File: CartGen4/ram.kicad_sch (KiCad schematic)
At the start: 1 part

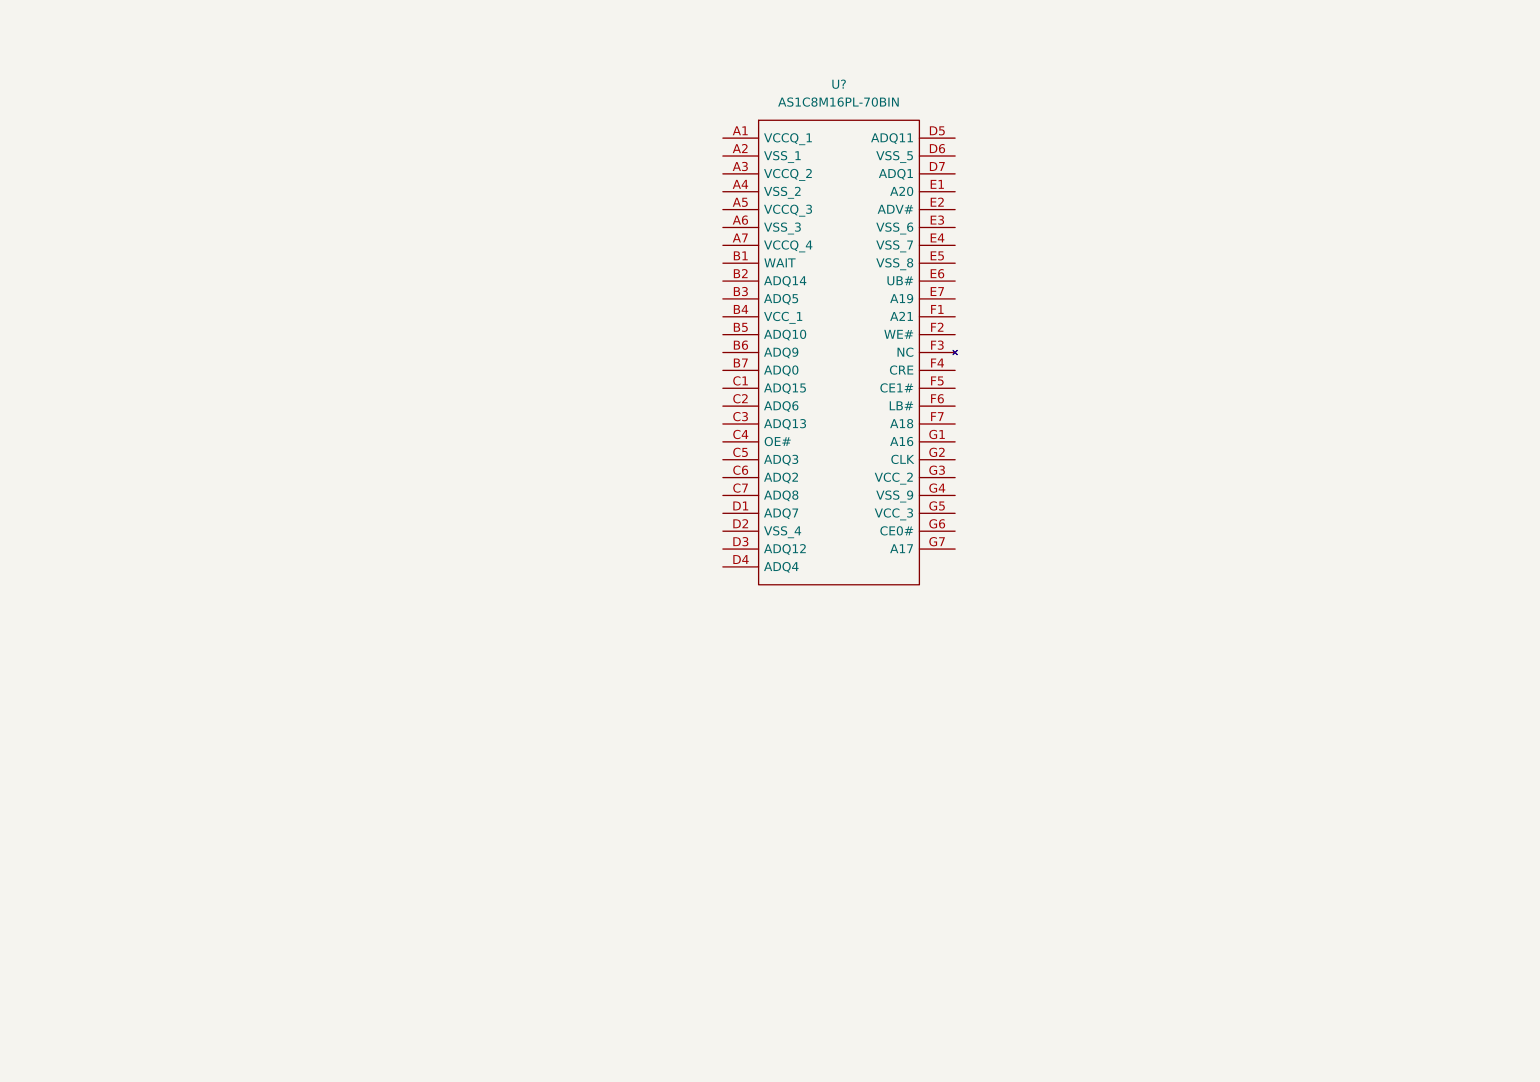
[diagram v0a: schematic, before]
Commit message: Added RAM and clock
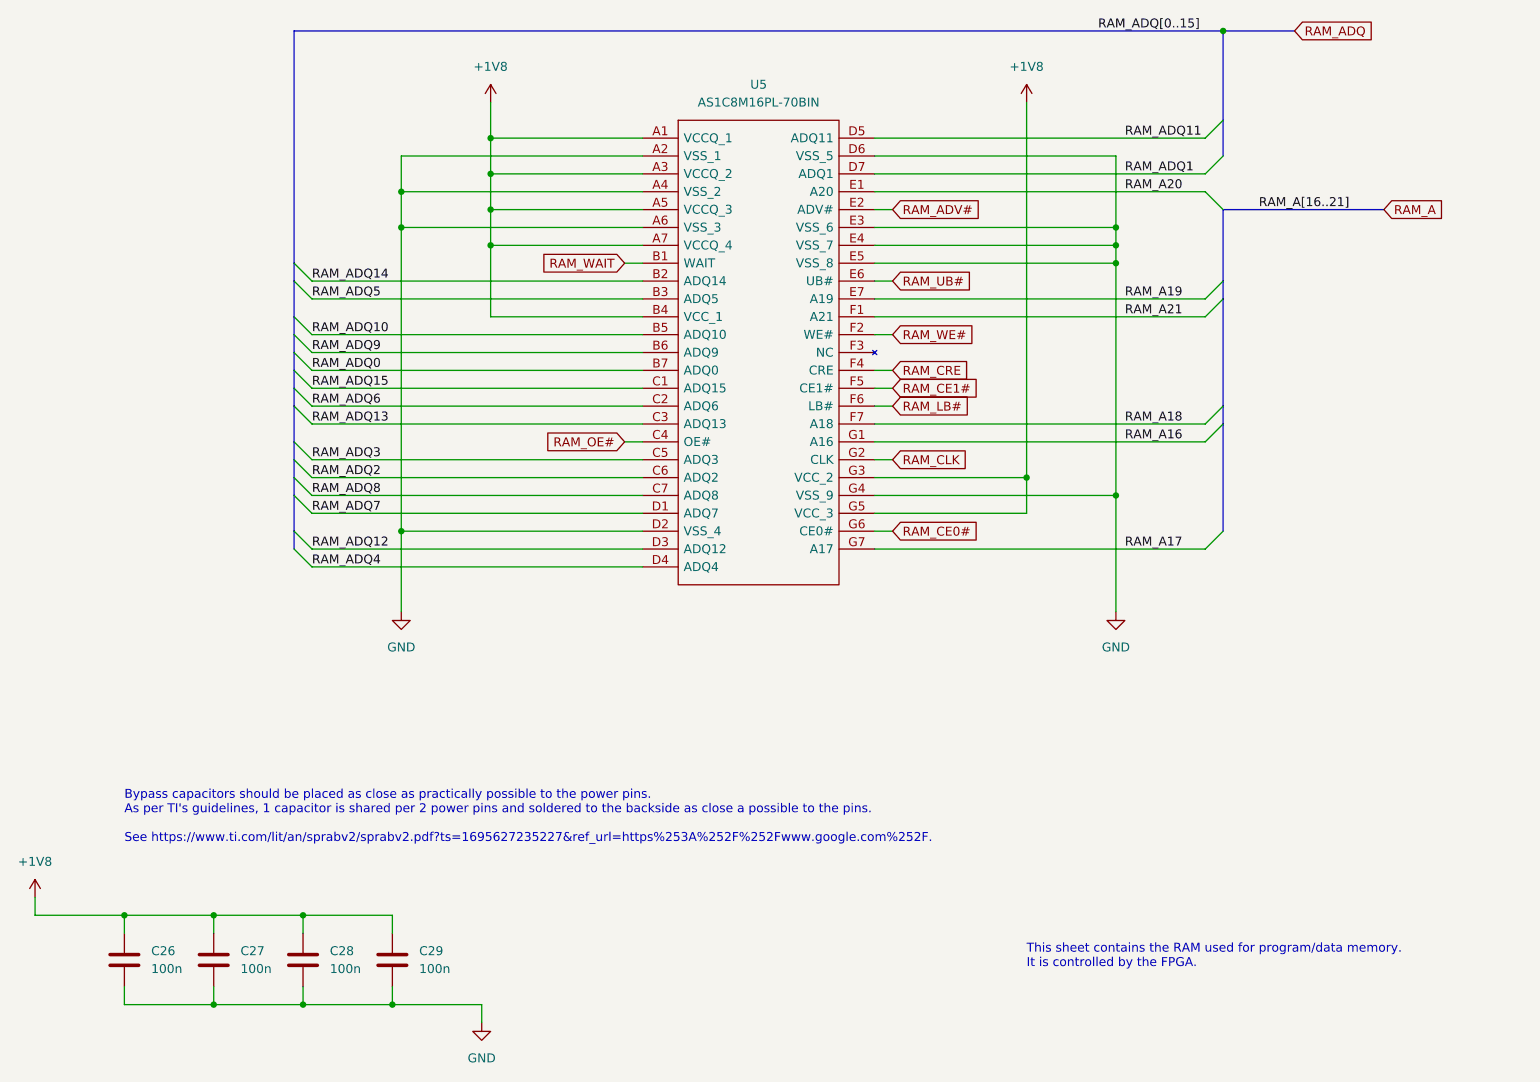
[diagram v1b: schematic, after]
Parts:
- added C26, C27, C28, C29: 100n, symbol Device:C
- gave numbers to parts that had none: 1
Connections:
- net +1V8: now reaches U5.A1 (VCCQ_1)
- net +1V8: now also U5.A3 (VCCQ_2), U5.A5 (VCCQ_3), U5.A7 (VCCQ_4), U5.B4 (VCC_1), U5.G3 (VCC_2), U5.G5 (VCC_3), C26.1, C27.1, C28.1, C29.1
- net GND: now reaches U5.A2 (VSS_1)
- net GND: now also U5.A4 (VSS_2), U5.A6 (VSS_3), U5.D2 (VSS_4), U5.D6 (VSS_5), U5.E3 (VSS_6), U5.E4 (VSS_7), U5.E5 (VSS_8), U5.G4 (VSS_9), C26.2, C27.2, C28.2, C29.2
- net RAM_WAIT: now reaches U5.B1 (WAIT)
- net RAM_ADQ14: now reaches U5.B2 (ADQ14)
- net RAM_ADQ5: now reaches U5.B3 (ADQ5)
- net RAM_ADQ10: now reaches U5.B5 (ADQ10)
- net RAM_ADQ9: now reaches U5.B6 (ADQ9)
- net RAM_ADQ0: now reaches U5.B7 (ADQ0)
- net RAM_ADQ15: now reaches U5.C1 (ADQ15)
- net RAM_ADQ6: now reaches U5.C2 (ADQ6)
- net RAM_ADQ13: now reaches U5.C3 (ADQ13)
- net RAM_OE#: now reaches U5.C4 (OE#)
- net RAM_ADQ3: now reaches U5.C5 (ADQ3)
- net RAM_ADQ2: now reaches U5.C6 (ADQ2)
- net RAM_ADQ8: now reaches U5.C7 (ADQ8)
- net RAM_ADQ7: now reaches U5.D1 (ADQ7)
- net RAM_ADQ12: now reaches U5.D3 (ADQ12)
- net RAM_ADQ4: now reaches U5.D4 (ADQ4)
- net RAM_ADQ11: now reaches U5.D5 (ADQ11)
- net RAM_ADQ1: now reaches U5.D7 (ADQ1)
- net RAM_A20: now reaches U5.E1 (A20)
- net RAM_ADV#: now reaches U5.E2 (ADV#)
- net RAM_UB#: now reaches U5.E6 (UB#)
- net RAM_A19: now reaches U5.E7 (A19)
- net RAM_A21: now reaches U5.F1 (A21)
- net RAM_WE#: now reaches U5.F2 (WE#)
- net RAM_CRE: now reaches U5.F4 (CRE)
- net RAM_CE1#: now reaches U5.F5 (CE1#)
- net RAM_LB#: now reaches U5.F6 (LB#)
- net RAM_A18: now reaches U5.F7 (A18)
- net RAM_A16: now reaches U5.G1 (A16)
- net RAM_CLK: now reaches U5.G2 (CLK)
- net RAM_CE0#: now reaches U5.G6 (CE0#)
- net RAM_A17: now reaches U5.G7 (A17)
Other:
- note added: "Bypass capacitors should be placed as close as practically possible to the power pins. As per TI's guidelines, 1 capacitor is shared per 2 power pins and soldered to the backside as close a possible to the pins. See https://www.ti.com/lit/an/sprabv2/sprabv2.pdf?ts=1695627235227&ref_url=https%253A%252F%252Fwww.google.com%252F."
- note added: "This sheet contains the RAM used for program/data memory. It is controlled by the FPGA."
- title: FPGA -> RAM
- moved on the sheet: U5

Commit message: Added copyright
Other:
- company: (none) -> © Elijah Almeida Coimbra
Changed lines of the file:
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@@
   (title_block
     (title "RAM")
+    (company "© Elijah Almeida Coimbra")
   )
   (junction (at 88.9 109.22) (diameter 0) (color 0 0 0 0)

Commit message: Fixed DRC
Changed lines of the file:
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@@
     )
   )
-  (global_label "RAM_ADQ" (shape input) (at 215.9 38.1 0) (fields_autoplaced)
+  (global_label "RAM_ADQ[0..15]" (shape input) (at 215.9 38.1 0) (fields_autoplaced)
     (effects (font (size 1.27 1.27)) (justify left))
-    (property "Intersheet References" "${INTERSHEET_REFS}" (id 0) (at 226.7798 38.0206 0)
+    (property "Intersheet References" "${INTERSHEET_REFS}" (id 0) (at 233.3112 38.0206 0)
       (effects (font (size 1.27 1.27)) (justify left) hide)
     )
@@
     )
   )
-  (global_label "RAM_A" (shape input) (at 228.6 63.5 0) (fields_autoplaced)
+  (global_label "RAM_A[16..21]" (shape input) (at 228.6 63.5 0) (fields_autoplaced)
     (effects (font (size 1.27 1.27)) (justify left))
-    (property "Intersheet References" "${INTERSHEET_REFS}" (id 0) (at 236.8793 63.4206 0)
+    (property "Intersheet References" "${INTERSHEET_REFS}" (id 0) (at 244.6202 63.4206 0)
       (effects (font (size 1.27 1.27)) (justify left) hide)
     )

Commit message: Cleaned up symbol fields
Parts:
- U5: Height 1 -> (none); MFN (none) -> Alliance Memory; MFP (none) -> AS1C8M16PL-70BIN; Manufacturer_Name Alliance Memory -> (none); Manufacturer_Part_Number AS1C8M16PL-70BIN -> (none); Mouser Part Number 913-AS1C8M16PL-70BIN -> (none); Mouser Price/Stock https://www.mouser.co.uk/ProductDetail/Alliance-Memory/AS1C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 -> (none)
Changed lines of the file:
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@@
       (effects (font (size 1.27 1.27)) (justify left) hide)
     )
-    (property "Height" "1" (id 5) (at 152.4 58.42 0)
+    (property "MFN" "Alliance Memory" (id 5) (at 152.4 66.04 0)
       (effects (font (size 1.27 1.27)) (justify left) hide)
     )
-    (property "Mouser Part Number" "913-AS1C8M16PL-70BIN" (id 6) (at 152.4 60.96 0)
+    (property "MFP" "AS1C8M16PL-70BIN" (id 6) (at 152.4 68.58 0)
       (effects (font (size 1.27 1.27)) (justify left) hide)
     )
-    (property "Mouser Price/Stock" "https://www.mouser.co.uk/ProductDetail/Alliance-Memory/AS1C8M16PL-70BIN?qs=byeeYqUIh0NST7XYuCr8lQ%3D%3D" (id 7) (at 152.4 63.5 0)
-      (effects (font (size 1.27 1.27)) (justify left) hide)
-    )
-    (property "Manufacturer_Name" "Alliance Memory" (id 8) (at 152.4 66.04 0)
-      (effects (font (size 1.27 1.27)) (justify left) hide)
-    )
-    (property "Manufacturer_Part_Number" "AS1C8M16PL-70BIN" (id 9) (at 152.4 68.58 0)
-      (effects (font (size 1.27 1.27)) (justify left) hide)
-    )

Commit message: Added symbol information to obvious stuff
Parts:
- C26, C27, C28, C29: Critical (none) -> N; Notes (none) -> Bypass capacitor for PWR/GND coupling.
- U5: Critical (none) -> Y; Notes (none) -> Used to contain running code.; Package ID (none) -> FBGA-49; Source (none) -> SPEC
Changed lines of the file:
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@@
+      (effects (font (size 1.27 1.27)) hide)
+    )
+    (property "Critical" "N" (id 4) (at 49.53 170.18 0)
+      (effects (font (size 1.27 1.27)) hide)
+    )
+    (property "Notes" "Bypass capacitor for PWR/GND coupling." (id 5) (at 49.53 170.18 0)
       (effects (font (size 1.27 1.27)) hide)
     )
@@
     (property "MFP" "AS1C8M16PL-70BIN" (id 6) (at 152.4 68.58 0)
       (effects (font (size 1.27 1.27)) (justify left) hide)
+    )
+    (property "Notes" "Used to contain running code." (id 7) (at 123.19 53.34 0)
+      (effects (font (size 1.27 1.27)) hide)
+    )
+    (property "Package ID" "FBGA-49" (id 8) (at 123.19 53.34 0)
+      (effects (font (size 1.27 1.27)) hide)
+    )
+    (property "Source" "SPEC" (id 9) (at 123.19 53.34 0)
+      (effects (font (size 1.27 1.27)) hide)
+    )
+    (property "Critical" "Y" (id 10) (at 123.19 53.34 0)
+      (effects (font (size 1.27 1.27)) hide)
     )
     (pin "A1")
@@
       (effects (font (size 1.27 1.27)) hide)
     )
+    (property "Critical" "N" (id 4) (at 87.63 170.18 0)
+      (effects (font (size 1.27 1.27)) hide)
+    )
+    (property "Notes" "Bypass capacitor for PWR/GND coupling." (id 5) (at 87.63 170.18 0)
+      (effects (font (size 1.27 1.27)) hide)
+    )
     (pin "1")
     (pin "2")
@@
       (effects (font (size 1.27 1.27)) hide)
     )
+    (property "Critical" "N" (id 4) (at 62.23 170.18 0)
+      (effects (font (size 1.27 1.27)) hide)
+    )
+    (property "Notes" "Bypass capacitor for PWR/GND coupling." (id 5) (at 62.23 170.18 0)
+      (effects (font (size 1.27 1.27)) hide)
+    )
     (pin "1")
     (pin "2")
@@
       (effects (font (size 1.27 1.27)) hide)
     )
+    (property "Critical" "N" (id 4) (at 74.93 170.18 0)
+      (effects (font (size 1.27 1.27)) hide)
+    )
+    (property "Notes" "Bypass capacitor for PWR/GND coupling." (id 5) (at 74.93 170.18 0)
+      (effects (font (size 1.27 1.27)) hide)
+    )

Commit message: Added more symbol information
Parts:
- C26, C27, C28, C29: Source (none) -> ANY
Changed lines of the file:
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@@
+      (effects (font (size 1.27 1.27)) hide)
+    )
+    (property "Source" "ANY" (id 6) (at 49.53 170.18 0)
       (effects (font (size 1.27 1.27)) hide)
     )
@@
       (effects (font (size 1.27 1.27)) hide)
     )
+    (property "Source" "ANY" (id 6) (at 87.63 170.18 0)
+      (effects (font (size 1.27 1.27)) hide)
+    )
     (pin "1")
     (pin "2")
@@
       (effects (font (size 1.27 1.27)) hide)
     )
+    (property "Source" "ANY" (id 6) (at 62.23 170.18 0)
+      (effects (font (size 1.27 1.27)) hide)
+    )
     (pin "1")
     (pin "2")
@@
       (effects (font (size 1.27 1.27)) hide)
     )
+    (property "Source" "ANY" (id 6) (at 74.93 170.18 0)
+      (effects (font (size 1.27 1.27)) hide)
+    )
